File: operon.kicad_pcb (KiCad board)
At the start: 2 copper layers, 50 x 50 mm, 109 parts, among them P1 USB, P3 MOD_SWD, P4 HEADER1, P5 HEADER2, P6 TC1, P7 TC2, P8 TC3, P9 TC4, Q1 AO3401A, Q2 ZXMN3A01F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

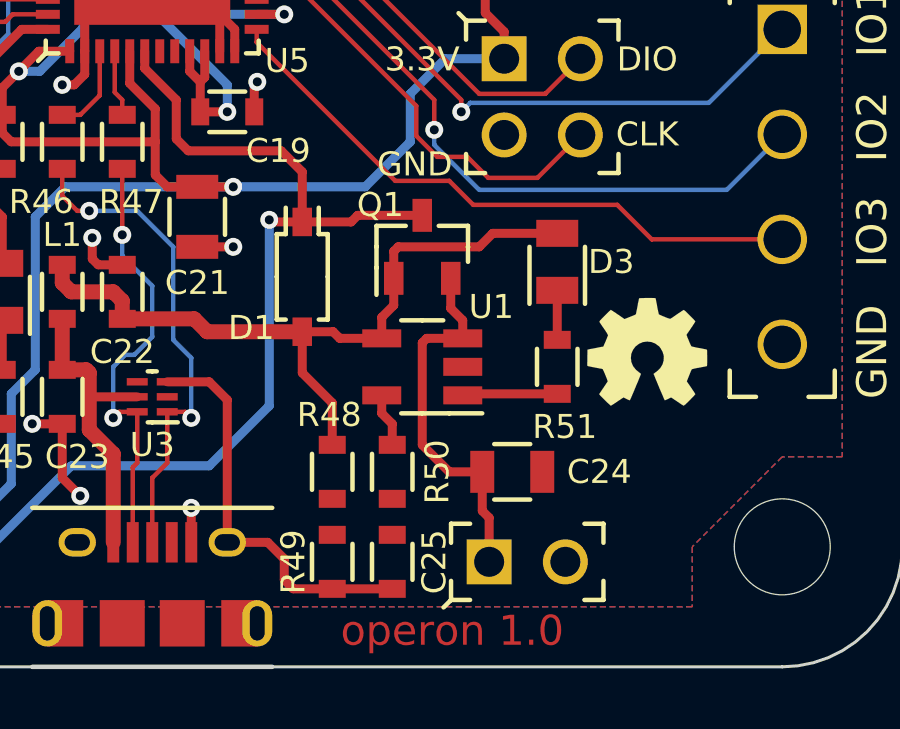
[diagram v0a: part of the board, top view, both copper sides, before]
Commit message: Reversed battery p-channel FET
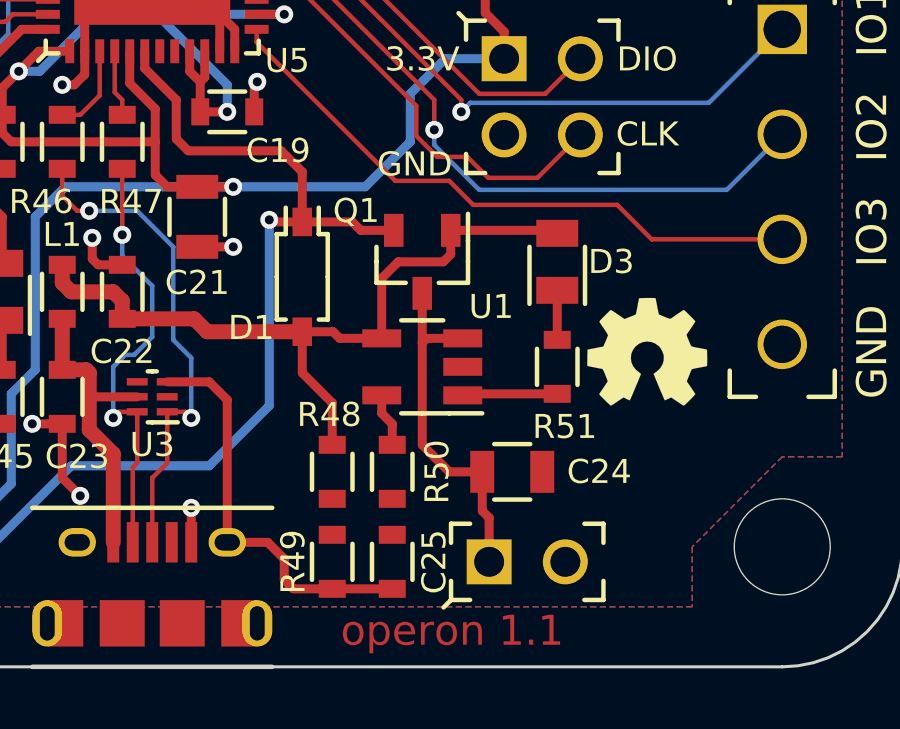
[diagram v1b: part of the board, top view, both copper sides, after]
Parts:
- moved Q1 0.50 mm to (134.0, 136.5), turned to 270 degrees
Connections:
- Q1 pad D: +5V -> N-0000023
- Q1 pad S: N-0000023 -> +5V
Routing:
- net +5V: track 76.8 -> 75.9 mm
- net N-0000023: track 12.4 -> 11.9 mm
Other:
- board text added: "operon 1.1"
- board text removed: "operon 1.0"
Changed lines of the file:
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@@
     (links 232)
     (no_connects 0)
-    (area 97.848334 91.921667 152.389287 155.385)
+    (area 99.949999 99.949999 150.050001 150.050001)
     (thickness 1.6)
     (drawings 54)
-    (tracks 722)
+    (tracks 719)
     (zones 0)
     (modules 109)
@@
   )
   (setup
-    (last_trace_width 0.15)
+    (last_trace_width 0.3)
     (user_trace_width 0.15)
     (user_trace_width 0.3)
@@
   )
   (module SOT190P230X100-3N (layer F.Cu)
-    (at 134 136 90)
-    (fp_text reference Q1 (at 1.4 -1.4 180) (layer F.SilkS)
+    (at 134 136.5 270)
+    (fp_text reference Q1 (at -1.7 2.2 360) (layer F.SilkS)
       (effects (font (size 0.8 0.8) (thickness 0.15)))
     )
-    (fp_text value AO3401A (at 0 0 90) (layer F.SilkS) hide
+    (fp_text value AO3401A (at 0 0 270) (layer F.SilkS) hide
       (effects (font (thickness 0.15)))
     )
@@
     (fp_line (start 1.85 1.8) (end 1.85 -1.8) (layer Eco2.User) (width 0.15))
     (fp_line (start 1.85 -1.8) (end -1.85 -1.8) (layer Eco2.User) (width 0.15))
-    (pad G smd rect (at -1.05 -0.95 90) (size 1.1 0.65)
+    (pad G smd rect (at -1.05 -0.95 270) (size 1.1 0.65)
       (layers F.Cu F.Paste F.Mask)
       (net 54 /VBUS2)
     )
-    (pad S smd rect (at -1.05 0.95 90) (size 1.1 0.65)
+    (pad S smd rect (at -1.05 0.95 270) (size 1.1 0.65)
       (layers F.Cu F.Paste F.Mask)
-      (net 66 N-0000023)
+      (net 3 +5V)
     )
-    (pad D smd rect (at 1.05 0 90) (size 1.1 0.65)
+    (pad D smd rect (at 1.05 0 270) (size 1.1 0.65)
       (layers F.Cu F.Paste F.Mask)
-      (net 3 +5V)
+      (net 66 N-0000023)
     )
   )
@@
     (effects (font (size 1 1) (thickness 0.15)))
   )
-  (gr_text "operon 1.0" (at 135 148.8) (layer F.Mask)
+  (gr_text "operon 1.1" (at 135 148.8) (layer F.Mask)
     (effects (font (size 1 1) (thickness 0.15)))
   )
-  (gr_text "operon 1.0" (at 135 148.8) (layer F.Cu)
+  (gr_text "operon 1.1" (at 135 148.8) (layer F.Cu)
     (effects (font (size 1 1) (thickness 0.15)))
   )
@@
   (segment (start 126.5 104) (end 125.9 104) (width 0.3) (layer F.Cu) (net 2))
   (segment (start 125.9 104) (end 125.65 103.75) (width 0.3) (layer F.Cu) (net 2))
+  (segment (start 130 135.17) (end 131.67 135.17) (width 0.3) (layer F.Cu) (net 3) (status 400000))
+  (segment (start 131.95 135.45) (end 133.05 135.45) (width 0.3) (layer F.Cu) (net 3) (status 800000))
+  (segment (start 131.67 135.17) (end 131.95 135.45) (width 0.3) (layer F.Cu) (net 3))
   (segment (start 104 119.75) (end 102.2 121.55) (width 0.3) (layer B.Cu) (net 3))
   (segment (start 128.97 135.17) (end 130 135.17) (width 0.3) (layer F.Cu) (net 3))
@@
   (segment (start 125.8 131.1) (end 124.75 130.05) (width 0.3) (layer F.Cu) (net 3))
   (segment (start 125.8 132.4) (end 125.8 131.1) (width 0.3) (layer F.Cu) (net 3))
-  (segment (start 134 134.95) (end 131.85 134.95) (width 0.3) (layer F.Cu) (net 3))
-  (segment (start 131.63 135.17) (end 130 135.17) (width 0.3) (layer F.Cu) (net 3))
-  (segment (start 131.85 134.95) (end 131.63 135.17) (width 0.3) (layer F.Cu) (net 3))
   (segment (start 128.48 128.25) (end 129.4 128.25) (width 0.3) (layer F.Cu) (net 4))
   (segment (start 124.9 126.5) (end 124.9 120.9) (width 0.3) (layer B.Cu) (net 4))
@@
   (segment (start 123.7 142.9) (end 122.9 142.1) (width 0.5) (layer F.Cu) (net 53))
   (segment (start 122 140.1) (end 122 138.4) (width 0.5) (layer F.Cu) (net 53))
+  (segment (start 134.95 135.45) (end 138.4 135.45) (width 0.3) (layer F.Cu) (net 54) (status C00000))
+  (segment (start 138.4 135.45) (end 138.5 135.55) (width 0.3) (layer F.Cu) (net 54) (status C00000))
+  (segment (start 132.65 139.05) (end 132.65 137.05) (width 0.3) (layer F.Cu) (net 54) (status 400000))
+  (segment (start 134.95 136.25) (end 134.95 135.45) (width 0.3) (layer F.Cu) (net 54) (status 800000))
+  (segment (start 134.7 136.5) (end 134.95 136.25) (width 0.3) (layer F.Cu) (net 54))
+  (segment (start 133.2 136.5) (end 134.7 136.5) (width 0.3) (layer F.Cu) (net 54))
+  (segment (start 132.65 137.05) (end 133.2 136.5) (width 0.3) (layer F.Cu) (net 54))
   (segment (start 130 138.83) (end 130 140.2) (width 0.3) (layer F.Cu) (net 54))
   (segment (start 131 141.2) (end 131 142.6) (width 0.3) (layer F.Cu) (net 54))
@@
   (segment (start 131.25 139.05) (end 132.65 139.05) (width 0.3) (layer F.Cu) (net 54))
   (segment (start 131.03 138.83) (end 131.25 139.05) (width 0.3) (layer F.Cu) (net 54))
-  (segment (start 132.65 139.05) (end 132.65 138.35) (width 0.3) (layer F.Cu) (net 54))
-  (segment (start 133.05 137.95) (end 133.05 137.05) (width 0.3) (layer F.Cu) (net 54))
-  (segment (start 132.65 138.35) (end 133.05 137.95) (width 0.3) (layer F.Cu) (net 54))
-  (segment (start 133.05 137.05) (end 133.05 136.15) (width 0.3) (layer F.Cu) (net 54))
-  (segment (start 133.05 136.15) (end 133.2 136) (width 0.3) (layer F.Cu) (net 54))
-  (segment (start 133.2 136) (end 135.9 136) (width 0.3) (layer F.Cu) (net 54))
-  (segment (start 135.9 136) (end 136.35 135.55) (width 0.3) (layer F.Cu) (net 54))
-  (segment (start 136.35 135.55) (end 138.5 135.55) (width 0.3) (layer F.Cu) (net 54))
   (segment (start 124 138.4) (end 126.4 138.4) (width 0.5) (layer F.Cu) (net 54))
   (segment (start 126.83 138.83) (end 130 138.83) (width 0.5) (layer F.Cu) (net 54))
@@
   (segment (start 115 110) (end 116.1 110) (width 0.3) (layer F.Cu) (net 55))
   (segment (start 138.5 137.45) (end 138.5 139.1) (width 0.3) (layer F.Cu) (net 56))
-  (segment (start 135.35 139.05) (end 135.35 138.45) (width 0.3) (layer F.Cu) (net 66))
-  (segment (start 134.95 138.05) (end 134.95 137.05) (width 0.3) (layer F.Cu) (net 66))
-  (segment (start 135.35 138.45) (end 134.95 138.05) (width 0.3) (layer F.Cu) (net 66))
+  (segment (start 134 139.2) (end 134 137.55) (width 0.3) (layer F.Cu) (net 66) (status 800000))
   (segment (start 136 143.5) (end 134.9 143.5) (width 0.3) (layer F.Cu) (net 66))
   (segment (start 134.15 139.05) (end 135.35 139.05) (width 0.3) (layer F.Cu) (net 66))
